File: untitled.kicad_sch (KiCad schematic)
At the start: 74 parts, among them U1 K210_C913414, U12 PCIE-67P42H, U4 XC6206P182MR_C347373, U5 GD25LQ128EWIGR, U6 TMI7003C, U7 SGM803-TXN3/TR_C5152602, U8 XC6206P302MR_C347375, X1 X322526MMB4SI

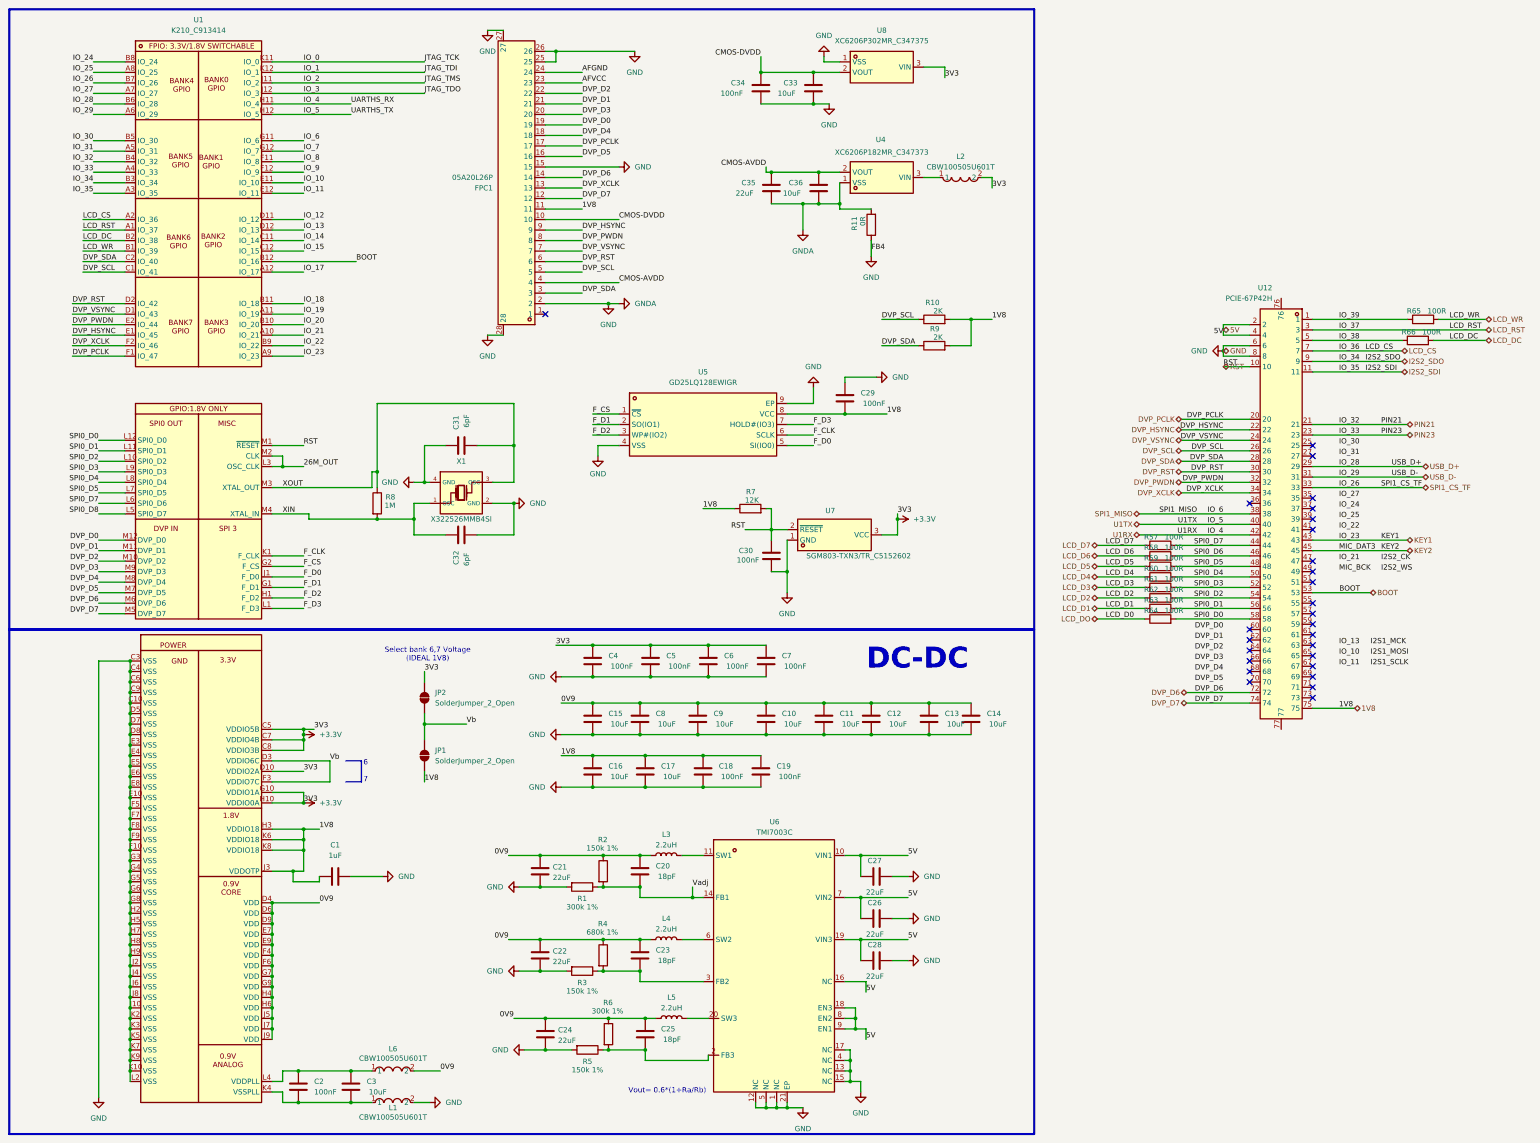
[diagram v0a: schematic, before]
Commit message: fios e vias lcd toutch botoes e o q mais estava conectado ao modulo m2 alem da coexao m2 com k210
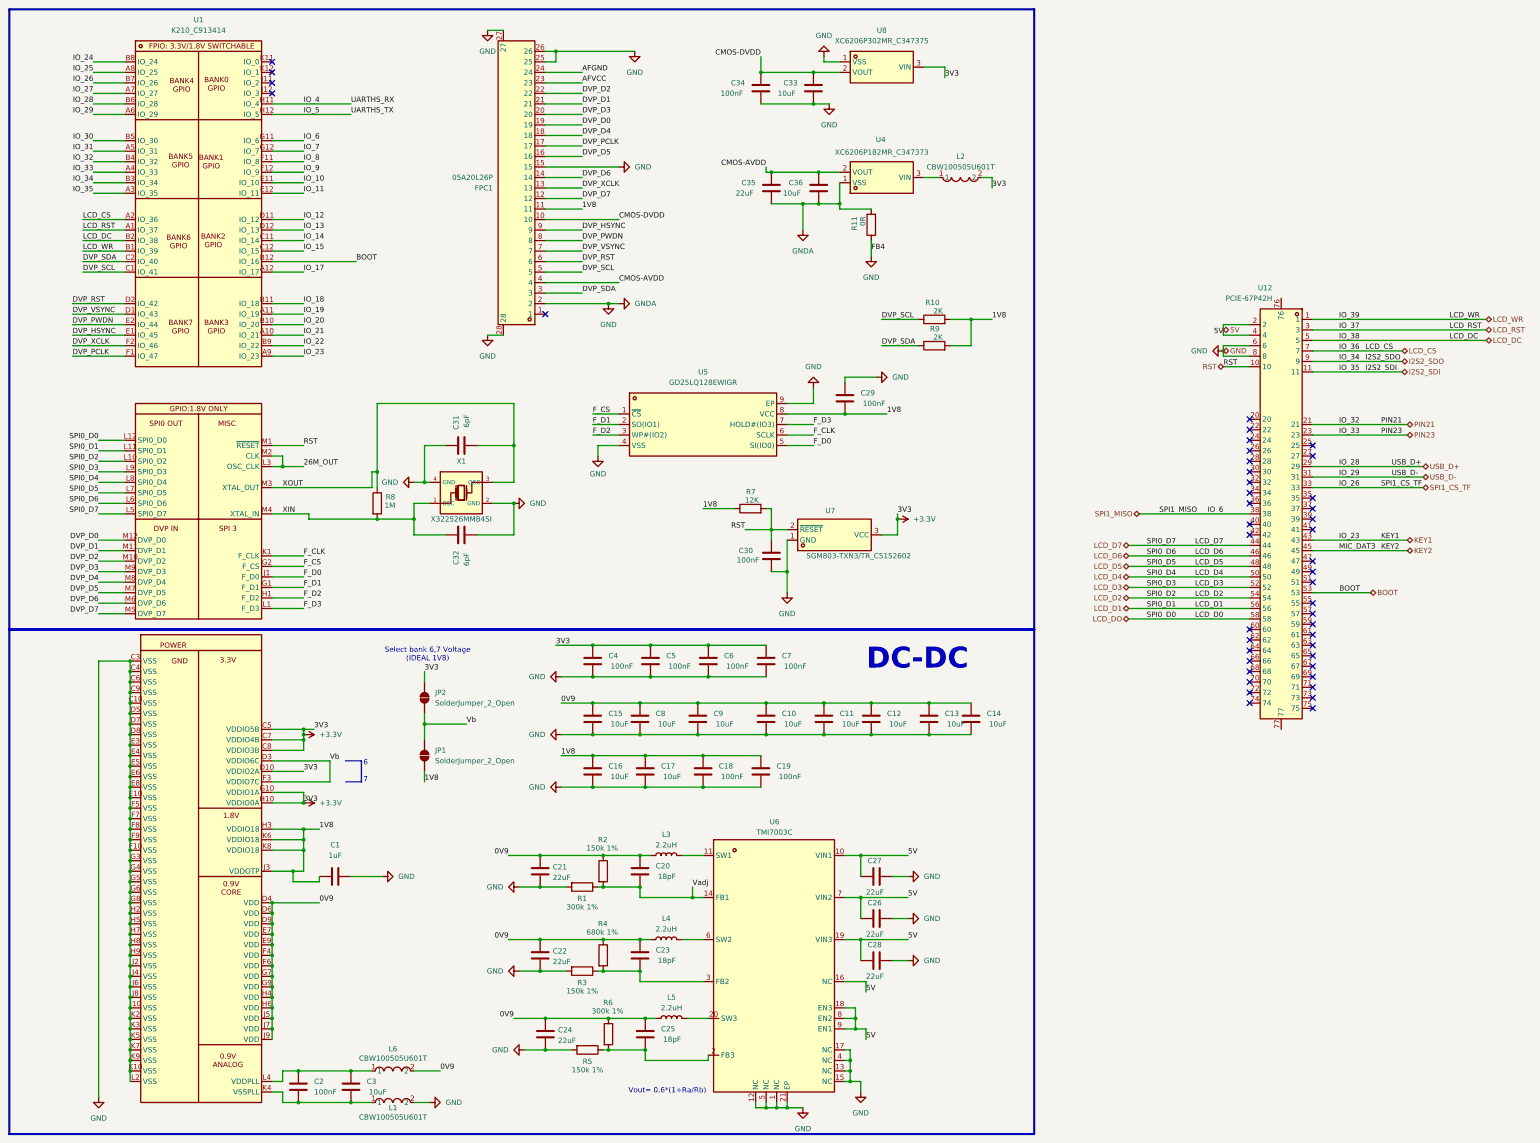
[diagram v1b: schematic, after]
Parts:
- removed R57, R58, R59, R60, R61, R62, R63, R64, R65, R66: 100R, Resistor_SMD:R_0201_0603Metric, symbol Device:R
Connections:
- net IO_38 is gone; now on net LCD_DC: U12.5
- net IO_39 is gone; now on net LCD_WR: U12.1
- net SPI0_D0 is gone; now on net LCD_DO: U1.L12 (SPI0_D0), U12.58
- net SPI0_D1 is gone; now on net LCD_D1: U1.L11 (SPI0_D1), U12.56
- net SPI0_D2 is gone; now on net LCD_D2: U1.L10 (SPI0_D2), U12.54
- net SPI0_D3 is gone; now on net LCD_D3: U1.L9 (SPI0_D3), U12.52
- net SPI0_D4 is gone; now on net LCD_D4: U1.L8 (SPI0_D4), U12.50
- net SPI0_D5 is gone; now on net LCD_D5: U1.L7 (SPI0_D5), U12.48
- net SPI0_D6 is gone; now on net LCD_D6: U12.46
- net SPI0_D8 is gone; now on net LCD_D7: U1.L5 (SPI0_D7)
- net 1V8: no longer U12.75
- net DVP_D6: no longer U12.72
- net DVP_D7: no longer U12.74
- net DVP_HSYNC: no longer U12.22
- net DVP_PCLK: no longer U12.20
- net DVP_PWDN: no longer U12.32
- net DVP_RST: no longer U12.30
- net DVP_SCL: no longer U12.26
- net DVP_SDA: no longer U12.28
- net DVP_VSYNC: no longer U12.24
- net DVP_XCLK: no longer U12.34
- net LCD_D6: now also U1.L6 (SPI0_D6)
- net LCD_D7: now also U12.44
- net IO_0: no longer names the net of U1.K11 (IO_0)
- net IO_1: no longer names the net of U1.K12 (IO_1)
- net IO_2: no longer names the net of U1.J11 (IO_2)
- net IO_3: no longer names the net of U1.J12 (IO_3)
- removed net SPI0_D7: U1.L6 (SPI0_D6), U12.44
- net U1RX: no longer names the net of U12.42
- net U1RX: no longer U1.H11 (IO_4)
- net U1TX: no longer names the net of U12.40
- net U1TX: no longer U1.H12 (IO_5)
- new net IO_4: U1.H11 (IO_4)
- new net IO_5: U1.H12 (IO_5)
- no-connect marks 27 -> 44
